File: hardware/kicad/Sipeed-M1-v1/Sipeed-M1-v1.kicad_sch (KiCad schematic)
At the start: 166 parts, among them IC1 TROPIC01_chip, J1 USB_C_, J2 JST Connector, J3 Conn_02x20_Odd_Even, J4 Conn_01x09_Pin, J5 Conn_02x03_Odd_Even, J6 Conn_01x20_Pin, Q2 FS8205A, SW1 SW_Push, SW10 SW_Push, SW11 SW_Push, SW12 SW_Push, SW13 SW_Push, SW14 SW_Push, SW15 SW_Push, SW16 SW_Push, SW2 SW_Push, SW3 SW_Push, SW4 SW_Push, SW5 SW_Push, SW6 SW_Push, SW7 SW_Push, SW8 SW_Push, SW9 SW_Push, U1 Sipeed-M1, U2 ESP32-S3-WROOM-1U-N8R8, U3 PAM2401YPADJ, U4 TPS63070RNMR, U5 MCP23017_SO, U6 BQ29700DSER, U7 USBLC6-2SC6, U8 MCP73871

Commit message: fixing output of the sipeed M1
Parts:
- removed J6: Conn_01x20_Pin, symbol Connector:Conn_01x20_Pin
- added J7: Conn_01x30_Pin, symbol Connector:Conn_01x30_Pin
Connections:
- net +3.3V_SYS: now also J7.1 (Pin_1)
- net GND: now also J7.17 (Pin_17), J7.2 (Pin_2), J7.28 (Pin_28), J7.29 (Pin_29), J7.30 (Pin_30), J7.9 (Pin_9)
- net M1_I2S_BCK: now also J7.27 (Pin_27)
- net M1_I2S_DA: now also J7.26 (Pin_26)
- net M1_I2S_WS: now also J7.25 (Pin_25)
- net M1_IO10: now also J7.7 (Pin_7)
- net M1_IO11: now also J7.8 (Pin_8)
- net M1_IO17: now also J7.10 (Pin_10)
- net M1_IO6: now also J7.3 (Pin_3)
- net M1_IO7: now also J7.4 (Pin_4)
- net M1_IO8: now also J7.5 (Pin_5)
- net M1_IO9: now also J7.6 (Pin_6)
- net M1_MIC0_BCK: now also J7.24 (Pin_24)
- net M1_MIC0_DATA: now also J7.23 (Pin_23)
- net M1_MIC0_WS: now also J7.22 (Pin_22)
- net M1_MIC_BCK: now also J7.11 (Pin_11)
- net M1_MIC_DAT0: now also J7.16 (Pin_16)
- net M1_MIC_DAT1: now also J7.15 (Pin_15)
- net M1_MIC_DAT2: now also J7.14 (Pin_14)
- net M1_MIC_DAT3: now also J7.13 (Pin_13)
- net M1_MIC_WS: now also J7.12 (Pin_12)
- net SPI_CS_M1: now also J7.21 (Pin_21)
- net SPI_MISO: now also J7.18 (Pin_18)
- net SPI_MOSI: now also J7.20 (Pin_20)
- net SPI_SCLK: now also J7.19 (Pin_19)
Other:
- note added: "CDC Badge Test"
- note added: "MCU SIPEED M1 (K210)"
- note removed: "MCU (OPTIONAL) SIPEED M1"
- moved on the sheet: C2, C3, C4, JP1, JP10, JP2, JP3, JP4, R10, R18, R24, R26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

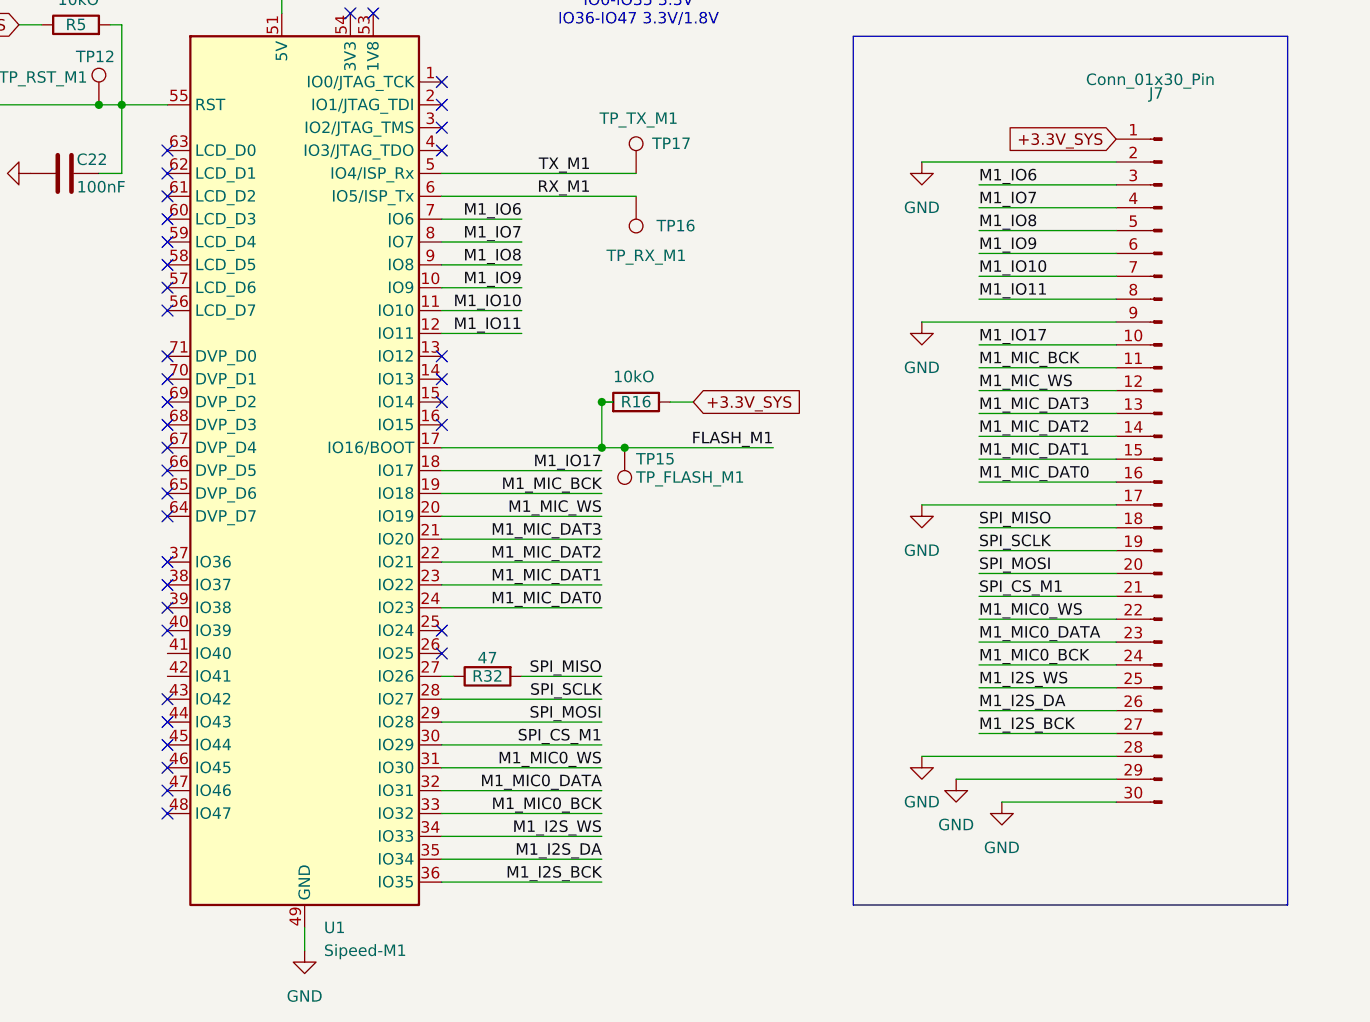
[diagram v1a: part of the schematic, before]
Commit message: revision of the 30pin output pin layout for the M1
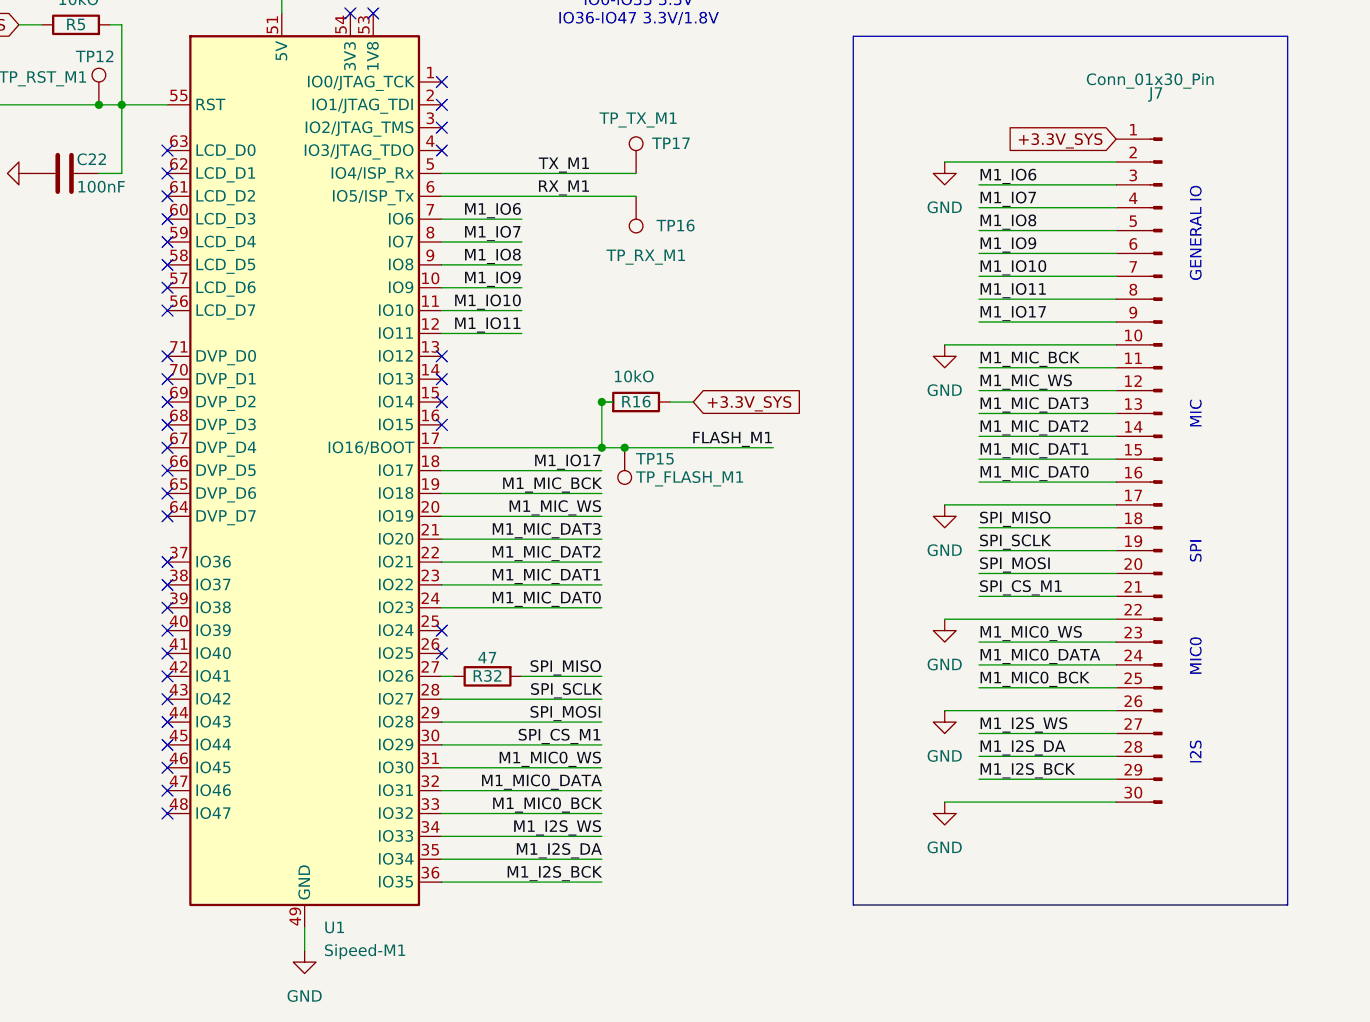
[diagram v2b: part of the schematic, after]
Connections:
- net GND: now also J7.10 (Pin_10), J7.22 (Pin_22), J7.26 (Pin_26); no longer J7.28 (Pin_28), J7.29 (Pin_29), J7.9 (Pin_9)
- net M1_I2S_BCK: now also J7.29 (Pin_29); no longer J7.27 (Pin_27)
- net M1_I2S_DA: now also J7.28 (Pin_28); no longer J7.26 (Pin_26)
- net M1_I2S_WS: now also J7.27 (Pin_27); no longer J7.25 (Pin_25)
- net M1_IO17: now also J7.9 (Pin_9); no longer J7.10 (Pin_10)
- net M1_MIC0_BCK: now also J7.25 (Pin_25); no longer J7.24 (Pin_24)
- net M1_MIC0_DATA: now also J7.24 (Pin_24); no longer J7.23 (Pin_23)
- net M1_MIC0_WS: now also J7.23 (Pin_23); no longer J7.22 (Pin_22)
- no-connect marks 43 -> 45
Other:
- note added: "GENERAL IO"
- note added: "I2S"
- note added: "MIC"
- note added: "MIC0"
- note added: "SPI"

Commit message: Added FPs and sorted the pcb board
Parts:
- IC1: footprint _M1_FP_lib:TROPIC01 QFN-32-1EP_4x4mm_P0.4mm_EP2.65x2.65mm -> _M1_FP_lib:TROPIC_QFN-32-1EP_4x4mm_P0.4mm_EP2.65x2.65mm
- J7: footprint (none) -> Connector_PinHeader_2.54mm:PinHeader_1x30_P2.54mm_Vertical
- U2: footprint _M1_FP_lib:XCVR_ESP32-S3-WROOM-1U-N8R8-NU -> _M1_FP_lib:ESP32-S3-WROOM-1U
- U3: footprint _M1_FP_lib:SON45P300X300X63-13N PAM2401 -> _M1_FP_lib:PAM2401_SON45P300X300X63-13N
- U6: footprint _M1_FP_lib:BQ29700DSER SON50P150X150X80-6N -> _M1_FP_lib:BQ29700_SON50P150X150X80-6N
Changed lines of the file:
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@@
 			)
 		)
-		(property "Footprint" "_M1_FP_lib:XCVR_ESP32-S3-WROOM-1U-N8R8-NU"
+		(property "Footprint" "_M1_FP_lib:ESP32-S3-WROOM-1U"
 			(at 294.64 349.25 0)
 			(effects
@@
 			)
 		)
-		(property "Footprint" "_M1_FP_lib:TROPIC01 QFN-32-1EP_4x4mm_P0.4mm_EP2.65x2.65mm"
+		(property "Footprint" "_M1_FP_lib:TROPIC_QFN-32-1EP_4x4mm_P0.4mm_EP2.65x2.65mm"
 			(at 88.9 252.73 0)
 			(effects
@@
 			)
 		)
-		(property "Datasheet" ""
+		(property "Datasheet" "https://github.com/tropicsquare/tropic01/blob/main/doc/datasheet/ODD_TR01_datasheet_revA9.pdf"
 			(at 88.9 224.79 0)
 			(effects
@@
 			)
 		)
-		(property "Footprint" "_M1_FP_lib:SON45P300X300X63-13N PAM2401"
+		(property "Footprint" "_M1_FP_lib:PAM2401_SON45P300X300X63-13N"
 			(at 82.55 134.62 0)
 			(effects
@@
 			)
 		)
-		(property "Footprint" ""
+		(property "Footprint" "Connector_PinHeader_2.54mm:PinHeader_1x30_P2.54mm_Vertical"
 			(at 172.72 341.63 0)
 			(effects
@@
 			)
 		)
-		(property "Footprint" "_M1_FP_lib:BQ29700DSER SON50P150X150X80-6N"
+		(property "Footprint" "_M1_FP_lib:BQ29700_SON50P150X150X80-6N"
 			(at 341.63 86.36 0)
 			(effects

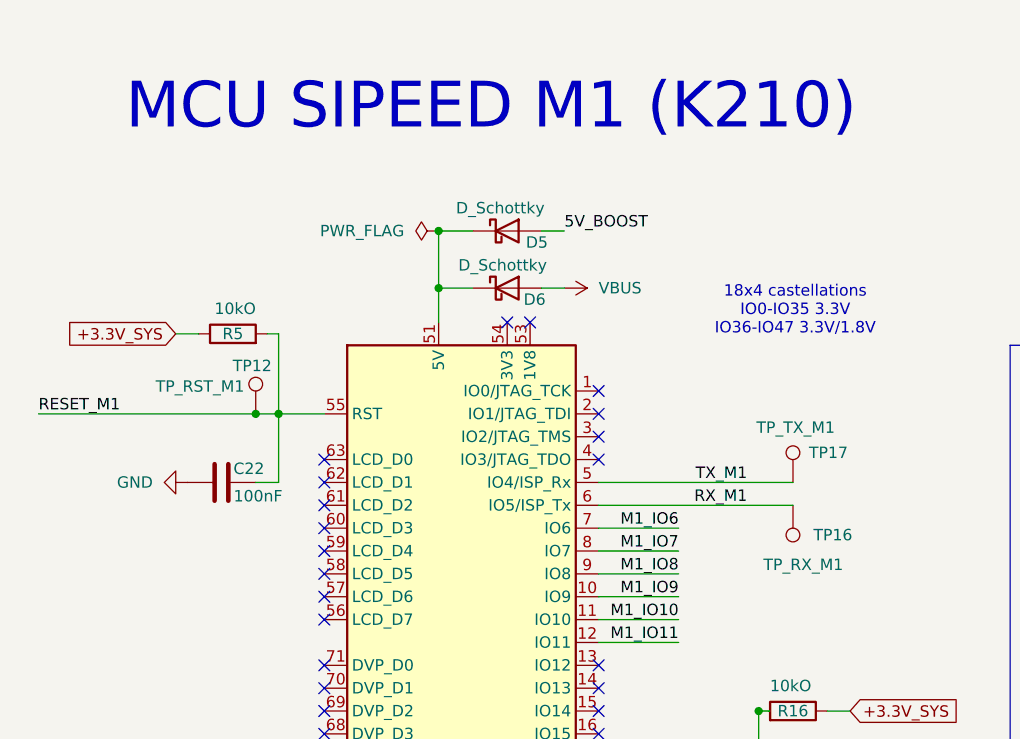
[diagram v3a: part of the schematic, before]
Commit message: updated pcb, added 3v3 and 1v8 net to m1, checked proper deletion of battery prot IC as lipos have their own
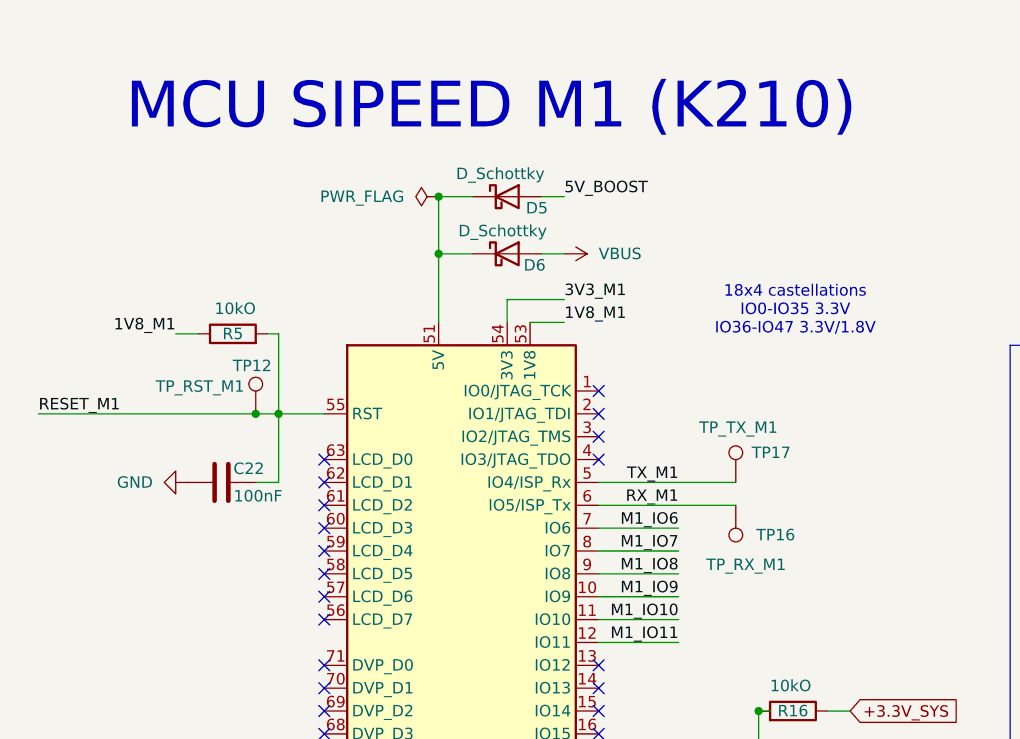
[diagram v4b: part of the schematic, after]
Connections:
- net +3.3V_SYS: no longer R5.1
- net 1V8_M1: now reaches U1.53 (1V8)
- net 1V8_M1: now also R5.1
- net 3V3_M1: now reaches U1.54 (3V3)
- no-connect marks 45 -> 43
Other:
- moved on the sheet: D5, D6, TP16, TP17
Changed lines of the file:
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@@
 	)
 	(junction
-		(at 74.93 281.94)
+		(at 74.93 278.13)
 		(diameter 0)
 		(color 0 0 0 0)
@@
 	)
 	(junction
-		(at 74.93 288.29)
+		(at 74.93 284.48)
 		(diameter 0)
 		(color 0 0 0 0)
@@
 	)
 	(no_connect
-		(at 82.55 292.1)
-	)
-	(no_connect
 		(at 90.17 67.31)
 	)
@@
 	)
 	(no_connect
-		(at 85.09 292.1)
-	)
-	(no_connect
 		(at 62.23 363.22)
 	)
@@
 	(wire
 		(pts
-			(xy 74.93 292.1) (xy 74.93 288.29)
+			(xy 74.93 292.1) (xy 74.93 284.48)
 		)
 		(stroke
@@
 	(wire
 		(pts
-			(xy 74.93 281.94) (xy 74.93 288.29)
+			(xy 74.93 278.13) (xy 74.93 284.48)
 		)
 		(stroke
@@
 	(wire
 		(pts
-			(xy 86.36 288.29) (xy 88.9 288.29)
+			(xy 86.36 284.48) (xy 88.9 284.48)
 		)
 		(stroke
@@
 	(wire
 		(pts
-			(xy 74.93 288.29) (xy 78.74 288.29)
+			(xy 74.93 284.48) (xy 78.74 284.48)
 		)
 		(stroke
@@
 	(wire
 		(pts
-			(xy 92.71 309.88) (xy 114.3 309.88)
+			(xy 92.71 309.88) (xy 107.95 309.88)
 		)
 		(stroke
@@
 	(wire
 		(pts
-			(xy 92.71 312.42) (xy 114.3 312.42)
+			(xy 92.71 312.42) (xy 107.95 312.42)
 		)
 		(stroke
@@
 	(wire
 		(pts
+			(xy 85.09 292.1) (xy 88.9 292.1)
+		)
+		(stroke
+			(width 0)
+			(type default)
+		)
+	)
+	(wire
+		(pts
 			(xy 300.99 81.28) (xy 314.96 81.28)
 		)
@@
 	(wire
 		(pts
+			(xy 82.55 292.1) (xy 82.55 289.56)
+		)
+		(stroke
+			(width 0)
+			(type default)
+		)
+	)
+	(wire
+		(pts
 			(xy 152.4 344.17) (xy 167.64 344.17)
 		)
@@
 	(wire
 		(pts
-			(xy 74.93 281.94) (xy 78.74 281.94)
+			(xy 74.93 278.13) (xy 78.74 278.13)
 		)
 		(stroke
@@
 	(wire
 		(pts
-			(xy 86.36 281.94) (xy 88.9 281.94)
+			(xy 86.36 278.13) (xy 88.9 278.13)
 		)
 		(stroke
@@
 	(wire
 		(pts
+			(xy 82.55 289.56) (xy 88.9 289.56)
+		)
+		(stroke
+			(width 0)
+			(type default)
+		)
+	)
+	(wire
+		(pts
 			(xy 314.96 86.36) (xy 314.96 88.9)
 		)
@@
 	)
 	(label "RX_M1"
-		(at 109.22 312.42 180)
+		(at 101.6 312.42 180)
 		(effects
 			(font
@@
 		)
 	)
+	(label "3V3_M1"
+		(at 88.9 289.56 0)
+		(effects
+			(font
+				(size 1.27 1.27)
+			)
+			(justify left bottom)
+		)
+	)
 	(label "M1_MIC_DAT3"
 		(at 152.4 336.55 0)
@@
 	)
 	(label "5V_BOOST"
-		(at 88.9 281.94 0)
+		(at 88.9 278.13 0)
 		(effects
 			(font
@@
 	)
 	(label "TX_M1"
-		(at 109.22 309.88 180)
+		(at 101.6 309.88 180)
 		(effects
 			(font
@@
 		)
 	)
+	(label "1V8_M1"
+		(at 88.9 292.1 0)
+		(effects
+			(font
+				(size 1.27 1.27)
+			)
+			(justify left bottom)
+		)
+	)
 	(label "M1_MIC_DAT3"
 		(at 110.49 350.52 180)
@@
 		)
 	)
+	(label "1V8_M1"
+		(at 45.72 293.37 180)
+		(effects
+			(font
+				(size 1.27 1.27)
+			)
+			(justify right bottom)
+		)
+	)
 	(label "M1_MIC0_WS"
 		(at 110.49 375.92 180)
@@
 	(global_label "+3.3V_SYS"
 		(shape input)
-		(at 45.72 293.37 180)
-		(fields_autoplaced yes)
-		(effects
-			(font
-				(size 1.27 1.27)
-			)
-			(justify right)
-		)
-		(property "Intersheetrefs" "${INTERSHEET_REFS}"
-			(at 32.5748 293.37 0)
-			(effects
-				(font
-					(size 1.27 1.27)
-				)
-				(justify right)
-				(hide yes)
-			)
-		)
-	)
-	(global_label "+3.3V_SYS"
-		(shape input)
 		(at 55.88 187.96 180)
 		(fields_autoplaced yes)
@@
 	(symbol
 		(lib_id "Device:D_Schottky")
-		(at 82.55 281.94 0)
+		(at 82.55 278.13 0)
 		(unit 1)
 		(exclude_from_sim no)
@@
 		(dnp no)
 		(property "Reference" "D5"
-			(at 85.852 283.21 0)
+			(at 85.852 279.4 0)
 			(effects
 				(font
@@
 		)
 		(property "Value" "D_Schottky"
-			(at 81.788 279.4 0)
+			(at 81.788 275.59 0)
 			(effects
 				(font
@@
 		)
 		(property "Footprint" "Diode_SMD:D_SOD-123F"
-			(at 82.55 281.94 0)
+			(at 82.55 278.13 0)
 			(effects
 				(font
@@
 		)
 		(property "Datasheet" "~"
-			(at 82.55 281.94 0)
+			(at 82.55 278.13 0)
 			(effects
 				(font
@@
 		)
 		(property "Description" "Schottky diode"
-			(at 82.55 281.94 0)
+			(at 82.55 278.13 0)
 			(effects
 				(font
@@
 	(symbol
 		(lib_id "Device:D_Schottky")
-		(at 82.55 288.29 0)
+		(at 82.55 284.48 0)
 		(unit 1)
 		(exclude_from_sim no)
@@
 		(dnp no)
 		(property "Reference" "D6"
-			(at 85.598 289.56 0)
+			(at 85.598 285.75 0)
 			(effects
 				(font
@@
 		)
 		(property "Value" "D_Schottky"
-			(at 82.042 285.75 0)
+			(at 82.042 281.94 0)
 			(effects
 				(font
@@
 		)
 		(property "Footprint" "Diode_SMD:D_SOD-123F"
-			(at 82.55 288.29 0)
+			(at 82.55 284.48 0)
 			(effects
 				(font
@@
 		)
 		(property "Datasheet" "~"
-			(at 82.55 288.29 0)
+			(at 82.55 284.48 0)
 			(effects
 				(font
@@
 		)
 		(property "Description" "Schottky diode"
-			(at 82.55 288.29 0)
+			(at 82.55 284.48 0)
 			(effects
 				(font
@@
 	(symbol
 		(lib_id "Connector:TestPoint")
-		(at 114.3 312.42 0)
+		(at 107.95 312.42 0)
 		(mirror x)
 		(unit 1)
@@
 		(dnp no)
 		(property "Reference" "TP16"
-			(at 120.904 315.722 0)
+			(at 114.554 315.722 0)
 			(effects
 				(font
@@
 		)
 		(property "Value" "TP_RX_M1"
-			(at 119.888 319.024 0)
+			(at 113.538 319.024 0)
 			(effects
 				(font
@@
 		)
 		(property "Footprint" "TestPoint:TestPoint_Pad_D2.0mm"
-			(at 119.38 312.42 0)
+			(at 113.03 312.42 0)
 			(effects
 				(font
@@
 		)
 		(property "Datasheet" "~"
-			(at 119.38 312.42 0)
+			(at 113.03 312.42 0)
 			(effects
 				(font
@@
 		)
 		(property "Description" "test point"
-			(at 114.3 312.42 0)
+			(at 107.95 312.42 0)
 			(effects
 				(font
@@
 	(symbol
 		(lib_id "power:PWR_FLAG")
-		(at 74.93 281.94 90)
+		(at 74.93 278.13 90)
 		(unit 1)
 		(exclude_from_sim no)
@@
 		(fields_autoplaced yes)
 		(property "Reference" "#FLG02"
-			(at 73.025 281.94 0)
+			(at 73.025 278.13 0)
 			(effects
 				(font
@@
 		)
 		(property "Value" "PWR_FLAG"
-			(at 71.12 281.9399 90)
+			(at 71.12 278.1299 90)
 			(effects
 				(font
@@
 		)
 		(property "Footprint" ""
-			(at 74.93 281.94 0)
+			(at 74.93 278.13 0)
 			(effects
 				(font
@@
 		)
 		(property "Datasheet" "~"
-			(at 74.93 281.94 0)
+			(at 74.93 278.13 0)
 			(effects
 				(font
@@
 		)
 		(property "Description" "Special symbol for telling ERC where power comes from"
-			(at 74.93 281.94 0)
+			(at 74.93 278.13 0)
 			(effects
 				(font
@@
 	(symbol
 		(lib_id "Connector:TestPoint")
-		(at 114.3 309.88 0)
+		(at 107.95 309.88 0)
 		(mirror y)
 		(unit 1)
@@
 		(dnp no)
 		(property "Reference" "TP17"
-			(at 116.078 306.578 0)
+			(at 109.728 306.578 0)
 			(effects
 				(font
@@
 		)
 		(property "Value" "TP_TX_M1"
-			(at 110.236 303.784 0)
+			(at 103.886 303.784 0)
 			(effects
 				(font
@@
 		)
 		(property "Footprint" "TestPoint:TestPoint_Pad_D2.0mm"
-			(at 109.22 309.88 0)
+			(at 102.87 309.88 0)
 			(effects
 				(font
@@
 		)
 		(property "Datasheet" "~"
-			(at 109.22 309.88 0)
+			(at 102.87 309.88 0)
 			(effects
 				(font
@@
 		)
 		(property "Description" "test point"
-			(at 114.3 309.88 0)
+			(at 107.95 309.88 0)
 			(effects
 				(font
@@
 	(symbol
 		(lib_id "power:VBUS")
-		(at 88.9 288.29 270)
+		(at 88.9 284.48 270)
 		(unit 1)
 		(exclude_from_sim no)
@@
 		(fields_autoplaced yes)
 		(property "Reference" "#PWR040"
-			(at 85.09 288.29 0)
+			(at 85.09 284.48 0)
 			(effects
 				(font
@@
 		)
 		(property "Value" "VBUS"
-			(at 92.71 288.2899 90)
+			(at 92.71 284.4799 90)
 			(effects
 				(font
@@
 		)
 		(property "Footprint" ""
-			(at 88.9 288.29 0)
+			(at 88.9 284.48 0)
 			(effects
 				(font
@@
 		)
 		(property "Datasheet" ""
-			(at 88.9 288.29 0)
+			(at 88.9 284.48 0)
 			(effects
 				(font
@@
 		)
 		(property "Description" "Power symbol creates a global label with name \"VBUS\""
-			(at 88.9 288.29 0)
+			(at 88.9 284.48 0)
 			(effects
 				(font

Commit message: Removed Protection IC from project
removed battery protection IC BQ29700DSER from our project, as the common lipos have their own anyways onboard.
updated and removed some other symbols and footprints too (removed the BQ29,
changed output pin to power output at 3v3 boost conv., removed unused)
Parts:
- removed C46: 100uF 10V Tant, Capacitor_Tantalum_SMD:CP_EIA-6032-28_Kemet-C, symbol Device:C_Polarized
- removed Q2: FS8205A, _M1_FP_lib:FS8205A TSSOP-8_3x3mm_P0.65mm, symbol _M1_symbols:FS8205A
- removed R17, R20: 100 O, Resistor_SMD:R_0603_1608Metric, symbol Device:R
- removed R19, R21: 100k, Resistor_SMD:R_0603_1608Metric, symbol Device:R
- removed TP2: TP_DOUT, TestPoint:TestPoint_Pad_D2.0mm, symbol Connector:TestPoint
- removed TP3: TP_COUT, TestPoint:TestPoint_Pad_D2.0mm, symbol Connector:TestPoint
- removed U6: BQ29700DSER, _M1_FP_lib:BQ29700_SON50P150X150X80-6N, symbol _M1_symbols:BQ29700DSER
- U2: footprint _M1_FP_lib:ESP32-S3-WROOM-1U -> _M1_FP_lib:XCVR_ESP32-S3-WROOM-1U-N8R8-NU
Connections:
- net CELL- is gone; now on net GND: C1.1, J2.2 (Pin_2)
- net +3.3V_SYS: no longer R16.1
- net 3V3_M1: now also R16.1
- net USB_D+: now also J1.A6 (D+), J1.B6 (D+), U7.3 (I/O2)
- no-connect marks 43 -> 42
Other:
- note added: "CELL-"
- note added: "With the removal of the battery prot. IC we also removed a 100uF 10V Tantalum Cap on the PACK+ line!"
- note removed: "BATTERY PROTECTION IC"
- note removed: "PACK-"
- moved on the sheet: C1, C10, C11, C12, C13, C18, C19, C23, C24, C29, C31, C32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
